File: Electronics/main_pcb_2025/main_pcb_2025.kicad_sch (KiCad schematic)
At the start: 68 parts, among them J1 PI40HAT, J10 Conn_01x02_Male, J11 Conn_01x02_Male, J12 Conn_01x02_Male, J13 Conn_01x02_Male, J15 Conn_01x02_Male, J16 Conn_01x02_Male, J17 Conn_01x03_Male, J18 Conn_01x03_Male, J2 Conn_01x02_Male, J2 Conn_01x04_Male, J20 Conn_01x05, J21 Conn_01x05, J22 Conn_01x05, J23 22-03-5035, J24 Conn_01x02_Male, J25 Conn_01x02_Male, J26 Conn_01x02_Male, J27 Conn_01x02_Male, J3 Conn_01x02_Male, J4 Conn_01x02_Male, J5 Conn_01x02_Male, J6 Conn_01x02_Male, J8 Conn_01x02_Male, J9 22-03-5035, P1 R-78Bxx-2.0, P2 Amazon 10A stepdown, Q1 NVTR4503NT1G, Q2 NVTR4503NT1G, Q3 NVTR4503NT1G, Q4 NVTR4503NT1G, Q5 NVTR4503NT1G, Q6 NVTR4503NT1G, Q7 NVTR4503NT1G, Q8 NVTR4503NT1G, U1 SN74LVC1G125DBVR, U2 SN74LVC1G04DBVR, U4 Pololu_MAX14870, U6 Pololu_MAX14870, U7 SN74AHCT1G126DBVR, U8 PCA9635

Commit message: Update main robot PCB
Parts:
- removed D1, D2: LED, LED_THT:LED_D3.0mm, symbol Device:LED
- removed J2, J3, J4: Conn_01x02_Male, MiAM:XT30UM, symbol Connector:Conn_01x02_Male
- removed J2 (x2): Conn_01x04_Male, Connector_JST:JST_SH_SM04B-SRSS-TB_1x04-1MP_P1.00mm_Horizontal, symbol Connector:Conn_01x04_Male
- removed J20, J21, J22: Conn_01x05, Connector_PinHeader_2.54mm:PinHeader_1x05_P2.54mm_Vertical, symbol Connector_Generic:Conn_01x05
- removed P1: R-78Bxx-2.0, MiAM:CONV_R-78Bxx-2.0, symbol MiAM:R-78Bxx-2.0
- removed P2: Amazon 10A stepdown, MiAM:StepDown10A, symbol MiAM:Amazon 10A stepdown
- removed R2, R3: R, Resistor_SMD:R_0805_2012Metric, symbol Device:R
- removed RN1: 47k, Resistor_THT:R_Array_SIP9, symbol Device:R_Network08
- added IC1: PCA9546AD, MiAM:SOIC127P600X175-16N, symbol MiAM:PCA9546AD
- added J14: Conn_01x02_Pin, MiAM:PogoPin_2.54, symbol Connector:Conn_01x02_Pin
- added J2, J28, J29, J3, J30, J4: 9801-0-15-15-23-27-10-0, MiAM:9801015152327100, symbol MiAM:9801-0-15-15-23-27-10-0
- added J20, J21, J22, J33: Conn_01x04_Male, Connector_JST:JST_SH_SM04B-SRSS-TB_1x04-1MP_P1.00mm_Horizontal, symbol Connector:Conn_01x04_Male
- added J31, J32: 22-03-5035, MiAM:SHDR3W60P0X250_1X3_990X490X590P, symbol MiAM:22-03-5035
- added R1: 10k, Resistor_SMD:R_0805_2012Metric, symbol Device:R
- added R11: 4k, Resistor_SMD:R_0805_2012Metric, symbol Device:R
- added RN1: EXB-2HV472JV, MiAM:EXB2HV_1, symbol MiAM:EXB-2HV473JV
- added RN3: EXB-2HV473JV, MiAM:EXB2HV_1, symbol MiAM:EXB-2HV473JV
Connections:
- net +24V: now also J30.1
- net +3.3V: now also U8.24 (A5), U8.25 (A6), IC1.16 (VCC), J20.2 (Pin_2), J21.2 (Pin_2), J22.2 (Pin_2), J33.2 (Pin_2), R1.2, R11.2, RN1.10, RN1.11, RN1.12, RN1.13, RN1.14, RN1.15, RN1.16, RN1.9
- net +5V: now also J4.1
- net +7.5V: now also J2.1
- net GND: now also JP1.3 (B), IC1.13 (A2), IC1.2 (A1), IC1.8 (GND), J20.1 (Pin_1), J21.1 (Pin_1), J22.1 (Pin_1), J28.1, J29.1, J31.3, J32.3, J33.1 (Pin_1), RN3.10, RN3.11, RN3.12, RN3.13, RN3.14, RN3.15, RN3.16, RN3.9; no longer U8.24 (A5), U8.25 (A6)
- net I2C SCL: now also IC1.14 (SCL), J14.1 (Pin_1)
- net I2C SDA: now also IC1.15 (SDA), J14.2 (Pin_2)
- net S0: now also RN3.1
- net S1: now also RN3.2
- net S2: now also RN3.3
- net S3: now also RN3.4
- net S4: now also RN3.5
- net S5: now also RN3.6
- net S6: now also RN3.7
- net S7: now also RN3.8
- net TX_EN: now also U2.4; no longer JP1.2 (C)
- net UART_HalfDuplex: now also J31.1, J32.1
- net at JP1.1 (A): now also R1.1; no longer U2.4
- net Servo DIR: no longer names the net of J1.12 (BCM18)
- net Servo DIR: no longer JP1.3 (B)
- new net: IC1.3 (~{RESET}), R11.1
- new net +12V: J3.1, J31.2, J32.2
- new net A0: IC1.1 (A0), JP1.2 (C)
- new net SCL0: IC1.5 (SC0), J20.4 (Pin_4), RN1.2
- new net SCL1: IC1.7 (SC1), J22.4 (Pin_4), RN1.4
- new net SCL2: IC1.10 (SC2), J21.4 (Pin_4), RN1.6
- new net SCL3: IC1.12 (SC3), J33.4 (Pin_4)
- new net SDA0: IC1.4 (SD0), J20.3 (Pin_3), RN1.1
- new net SDA1: IC1.6 (SD1), J22.3 (Pin_3), RN1.3
- new net SDA2: IC1.9 (SD2), J21.3 (Pin_3), RN1.5
- new net SDA3: IC1.11 (SD3), J33.3 (Pin_3), RN1.7
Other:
- note added: "0x68/6C"
- note added: "0x70/0x71"
- note added: "Power input"
- note removed: "Power distribution"
- note removed: "Qwiic"
- moved on the sheet: J2, J23, J5, J6, J9, R12, R14, R4, U1, U2, U7

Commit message: Update main PCB
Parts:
- removed C4: Conn_03x04, MiAM:Pin_Header_Straight_3x04_Pitch2.54mm, symbol MiAM:Conn_03x04
- removed J17, J18: Conn_01x03_Male, Connector_PinHeader_2.54mm:PinHeader_1x03_P2.54mm_Vertical, symbol Connector:Conn_01x03_Male
- added C3: Conn_03x06, MiAM:Pin_Header_Straight_3x06_Pitch2.54mm, symbol MiAM:Conn_03x06
- added JP3, JP4: SolderJumper_3_Open, Jumper:SolderJumper-3_P1.3mm_Open_Pad1.0x1.5mm, symbol Jumper:SolderJumper_3_Open
- I2C0: renamed from J20; footprint Connector_JST:JST_SH_SM04B-SRSS-TB_1x04-1MP_P1.00mm_Horizontal -> MiAM:JST_SH_SM04B-SRSS-TB_1x04-1MP_P1.00mm_Horizontal
- I2C1: renamed from J22; footprint Connector_JST:JST_SH_SM04B-SRSS-TB_1x04-1MP_P1.00mm_Horizontal -> MiAM:JST_SH_SM04B-SRSS-TB_1x04-1MP_P1.00mm_Horizontal
- I2C2: renamed from J21; footprint Connector_JST:JST_SH_SM04B-SRSS-TB_1x04-1MP_P1.00mm_Horizontal -> MiAM:JST_SH_SM04B-SRSS-TB_1x04-1MP_P1.00mm_Horizontal
- I2C3: renamed from J33; footprint Connector_JST:JST_SH_SM04B-SRSS-TB_1x04-1MP_P1.00mm_Horizontal -> MiAM:JST_SH_SM04B-SRSS-TB_1x04-1MP_P1.00mm_Horizontal
- J2: footprint Connector_JST:JST_SH_SM04B-SRSS-TB_1x04-1MP_P1.00mm_Horizontal -> MiAM:JST_SH_SM04B-SRSS-TB_1x04-1MP_P1.00mm_Horizontal
- J24: footprint Connector_Molex:Molex_PicoBlade_53047-0210_1x02_P1.25mm_Vertical -> MiAM:Molex_PicoBlade_53047-0210_1x02_P1.25mm_Vertical
- MOT1: renamed from J8; footprint Connector_Molex:Molex_PicoBlade_53047-0210_1x02_P1.25mm_Vertical -> MiAM:Molex_PicoBlade_53047-0210_1x02_P1.25mm_Vertical
- MOT2: renamed from J10; footprint Connector_Molex:Molex_PicoBlade_53047-0210_1x02_P1.25mm_Vertical -> MiAM:Molex_PicoBlade_53047-0210_1x02_P1.25mm_Vertical
- O0: renamed from J13; footprint Connector_Molex:Molex_PicoBlade_53047-0210_1x02_P1.25mm_Vertical -> MiAM:Molex_PicoBlade_53047-0210_1x02_P1.25mm_Vertical
- O1: renamed from J11; footprint Connector_Molex:Molex_PicoBlade_53047-0210_1x02_P1.25mm_Vertical -> MiAM:Molex_PicoBlade_53047-0210_1x02_P1.25mm_Vertical
- O2: renamed from J12; footprint Connector_Molex:Molex_PicoBlade_53047-0210_1x02_P1.25mm_Vertical -> MiAM:Molex_PicoBlade_53047-0210_1x02_P1.25mm_Vertical
- O3: renamed from J15; footprint Connector_Molex:Molex_PicoBlade_53047-0210_1x02_P1.25mm_Vertical -> MiAM:Molex_PicoBlade_53047-0210_1x02_P1.25mm_Vertical
- O4: renamed from J16; footprint Connector_Molex:Molex_PicoBlade_53047-0210_1x02_P1.25mm_Vertical -> MiAM:Molex_PicoBlade_53047-0210_1x02_P1.25mm_Vertical
- O5: renamed from J25; footprint Connector_Molex:Molex_PicoBlade_53047-0210_1x02_P1.25mm_Vertical -> MiAM:Molex_PicoBlade_53047-0210_1x02_P1.25mm_Vertical
- O6: renamed from J26; footprint Connector_Molex:Molex_PicoBlade_53047-0210_1x02_P1.25mm_Vertical -> MiAM:Molex_PicoBlade_53047-0210_1x02_P1.25mm_Vertical
- O7: renamed from J27; footprint Connector_Molex:Molex_PicoBlade_53047-0210_1x02_P1.25mm_Vertical -> MiAM:Molex_PicoBlade_53047-0210_1x02_P1.25mm_Vertical
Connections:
- net +24V: now also JP3.1 (A), JP4.1 (A)
- net +3.3V: now also C3.11, C3.14, C3.17, C3.2, C3.5, C3.8
- net +7.5V: now also JP3.3 (B), JP4.3 (B)
- net GND: now also C3.12, C3.15, C3.18, C3.3, C3.6, C3.9
- net GPIO 20: now also C3.1
- net GPIO 21: now also C3.4
- net GPIO 22: now also C3.7
- net GPIO 23: now also C3.10
- net GPIO 24: now also C3.13
- net GPIO 25: now also C3.16
- net S0: now also C1.4, RN3.8; no longer C1.1, RN3.1
- net S1: now also C1.3, RN3.7; no longer C1.2, RN3.2
- net S2: now also C1.2, RN3.6; no longer C1.3, RN3.3
- net S3: now also C1.1, RN3.5; no longer C1.4, RN3.4
- net S4: now also C2.4, RN3.4; no longer C2.1, RN3.5
- net S5: now also C2.3, RN3.3; no longer C2.2, RN3.6
- net S6: now also C2.2, RN3.2; no longer C2.3, RN3.7
- net S7: now also C2.1, RN3.1; no longer C2.4, RN3.8
- net SCL3: now also RN1.8
- net at U6.9 (Vin): now also JP3.2 (C)
- net at U4.9 (Vin): now also JP4.2 (C)

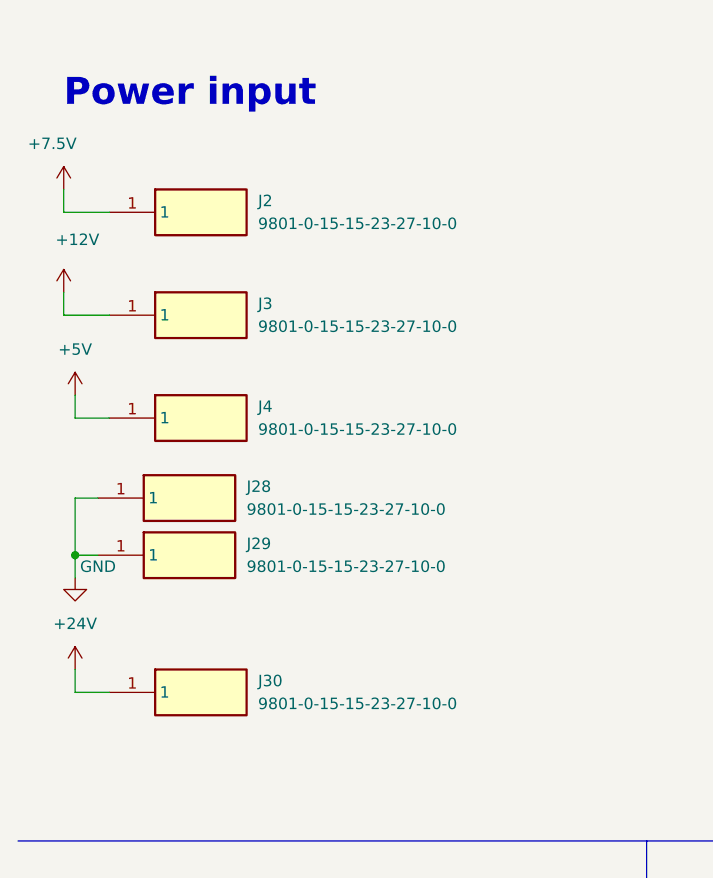
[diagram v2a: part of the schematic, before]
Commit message: PCB update - passes DRC
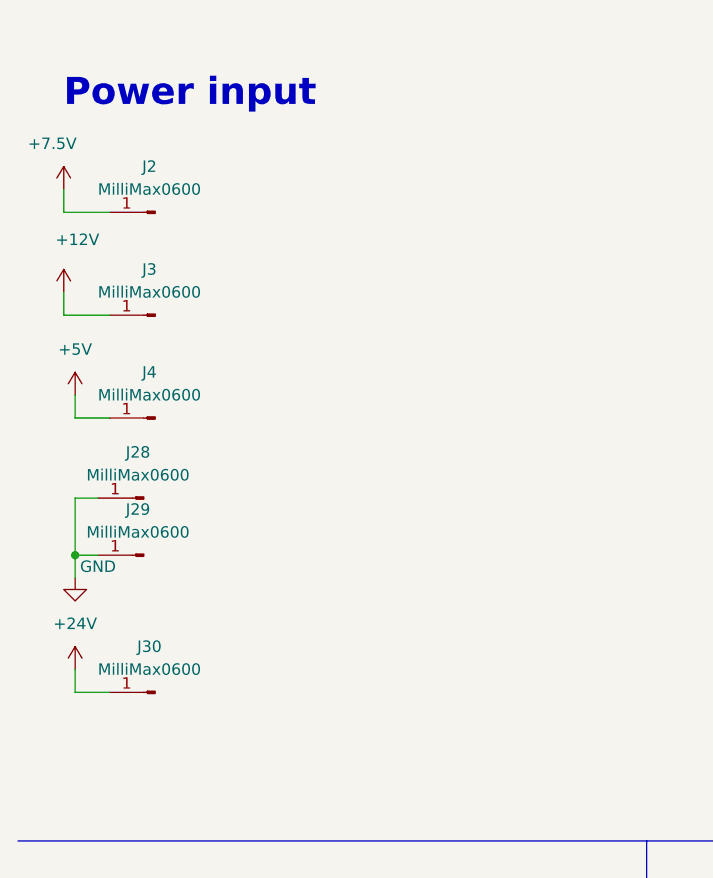
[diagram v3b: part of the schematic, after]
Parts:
- removed J2, J28, J29, J3, J30, J4: 9801-0-15-15-23-27-10-0, MiAM:9801015152327100, symbol MiAM:9801-0-15-15-23-27-10-0
- added J2, J28, J29, J3, J30, J4: MilliMax0600, MiAM:0600005150000, symbol Connector:Conn_01x01_Pin
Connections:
- net +12V: now also J3.1 (Pin_1)
- net +24V: now also J30.1 (Pin_1)
- net +5V: now also J4.1 (Pin_1)
- net +7.5V: now also J2.1 (Pin_1)
- net GND: now also J28.1 (Pin_1), J29.1 (Pin_1)

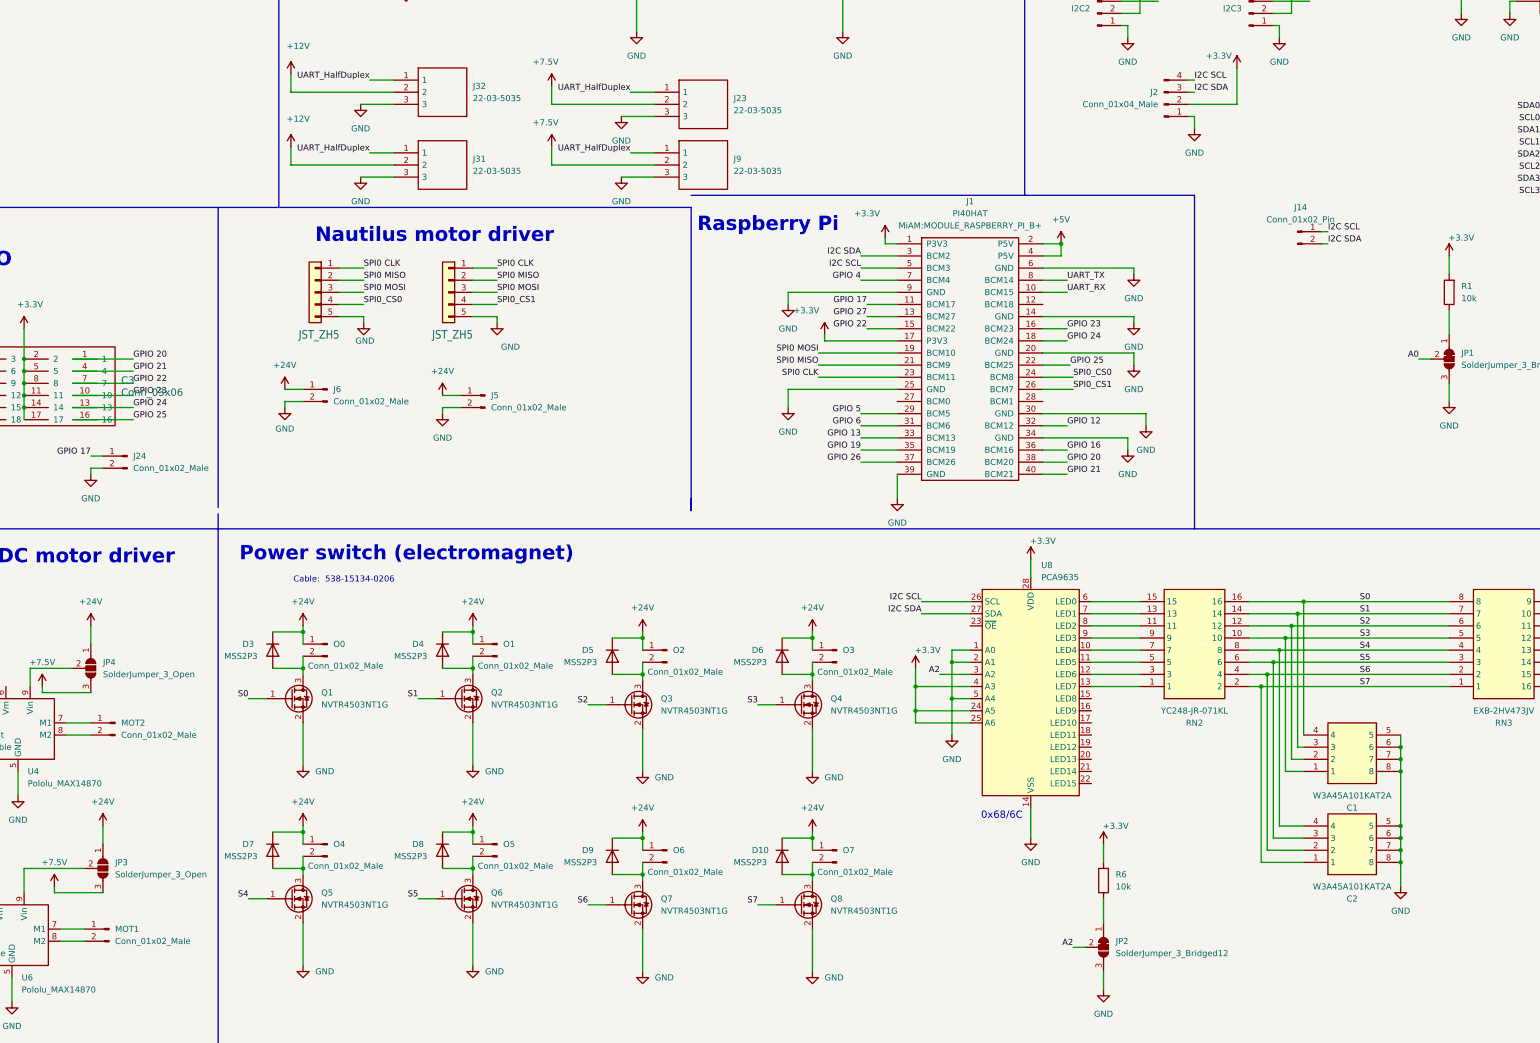
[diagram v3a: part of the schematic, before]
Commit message: Update ECAD library
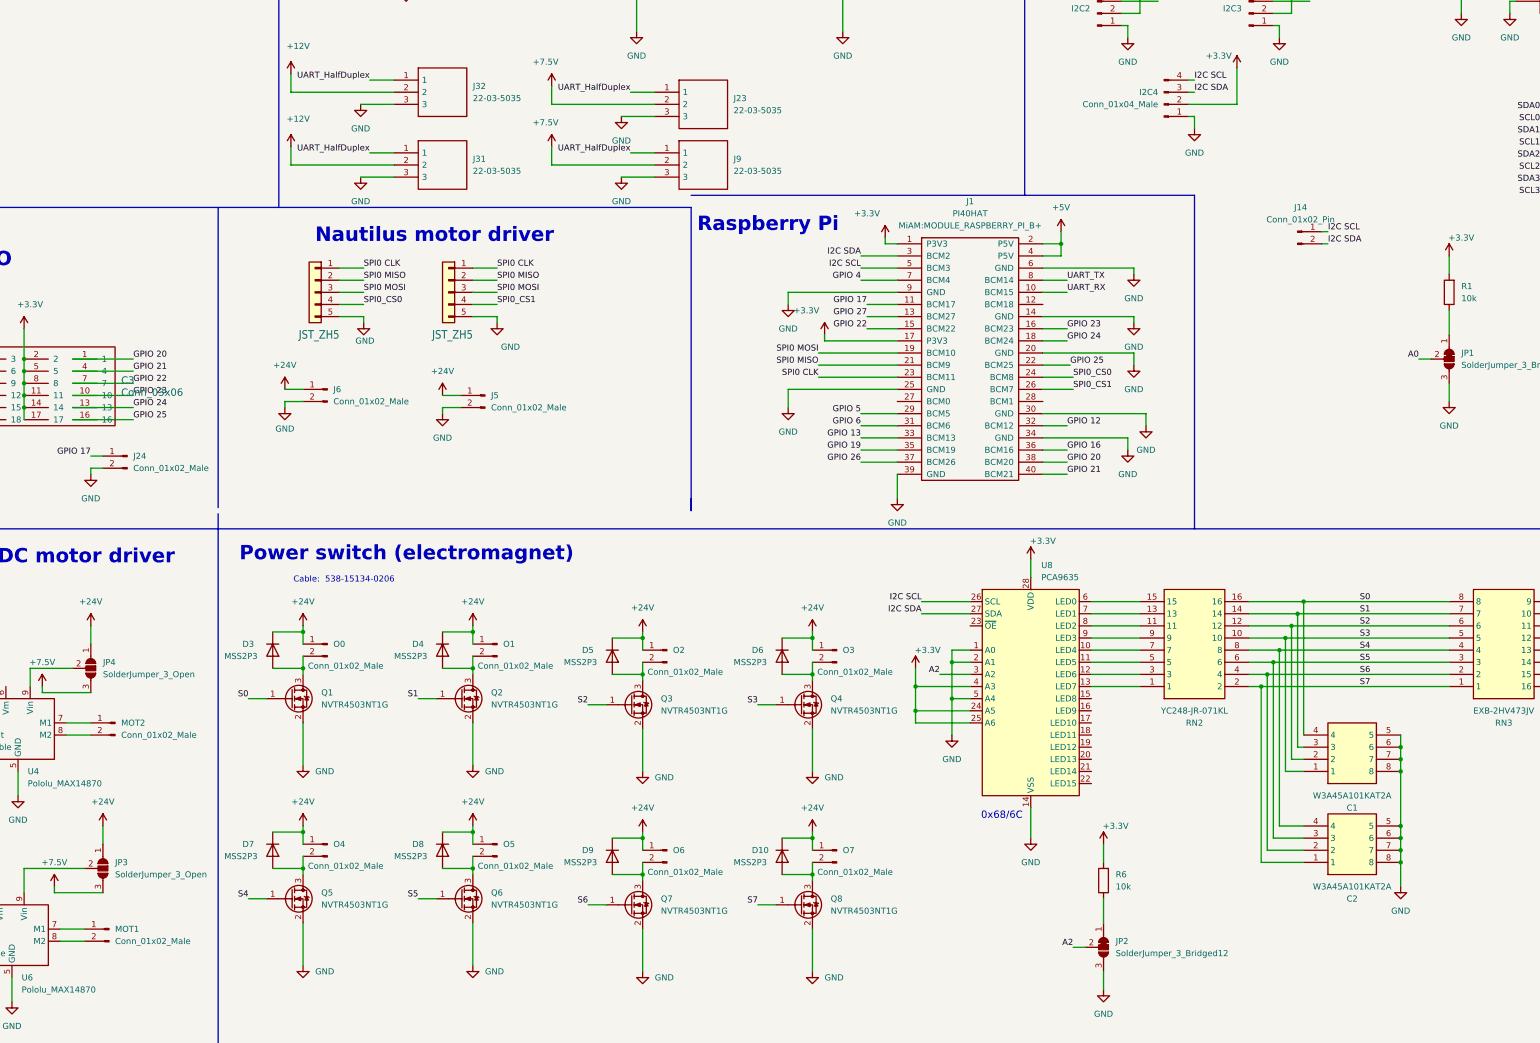
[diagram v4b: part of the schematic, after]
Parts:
- renumbered J2 to I2C4, SPI0 to SPI2
